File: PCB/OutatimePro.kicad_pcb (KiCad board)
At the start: 2 copper layers, 25.7 x 27.7 mm, 53 parts, among them IC1 PAM8904JPR, J1 USB_B_Micro_PCB_Edge_receptac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, J3 OSO_SWD, Q1 ALS-PT19-315C/L177/TR8, SW1 EVPAWED40, U1 ATSAML22N18A-CFUT, U2 MIC5365-3.3YMT, U3 USBLC6-2P6, U4 MAX40200ANS, U5 MAX40200ANS, U6 LIS2DW12TR, Y1 32.768kHz

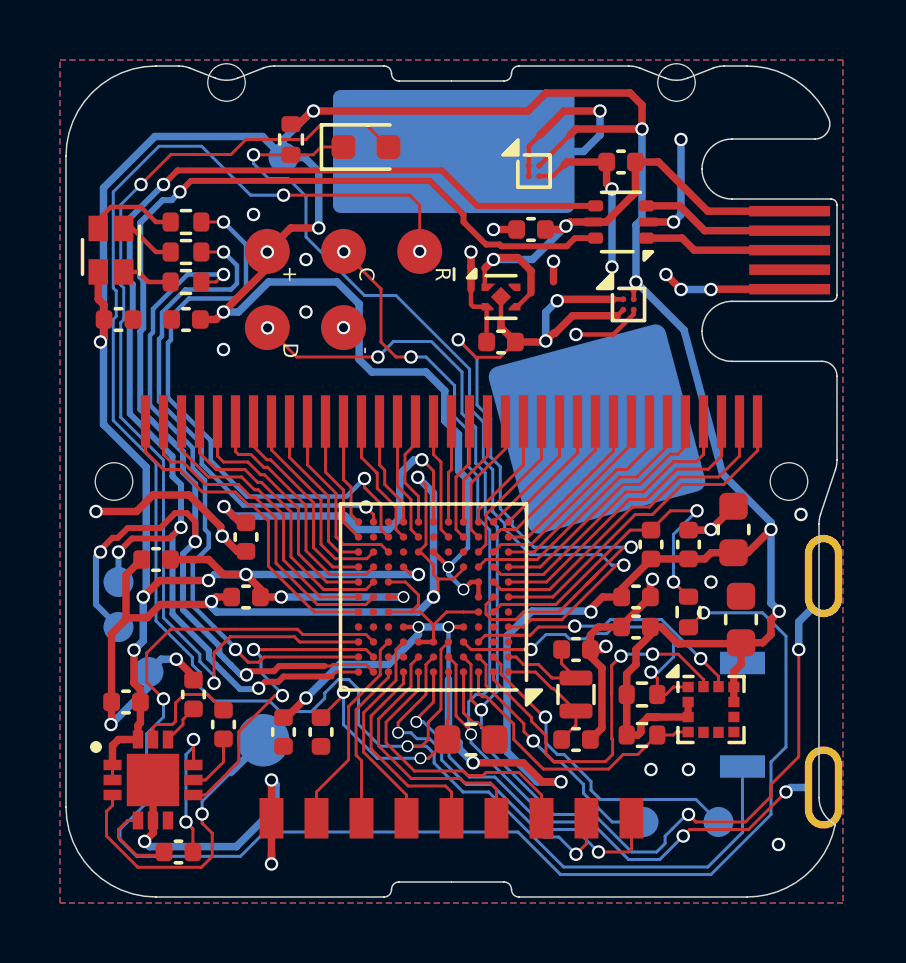
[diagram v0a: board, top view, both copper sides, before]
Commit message: move mcu to part where it fits & add promotional artwork
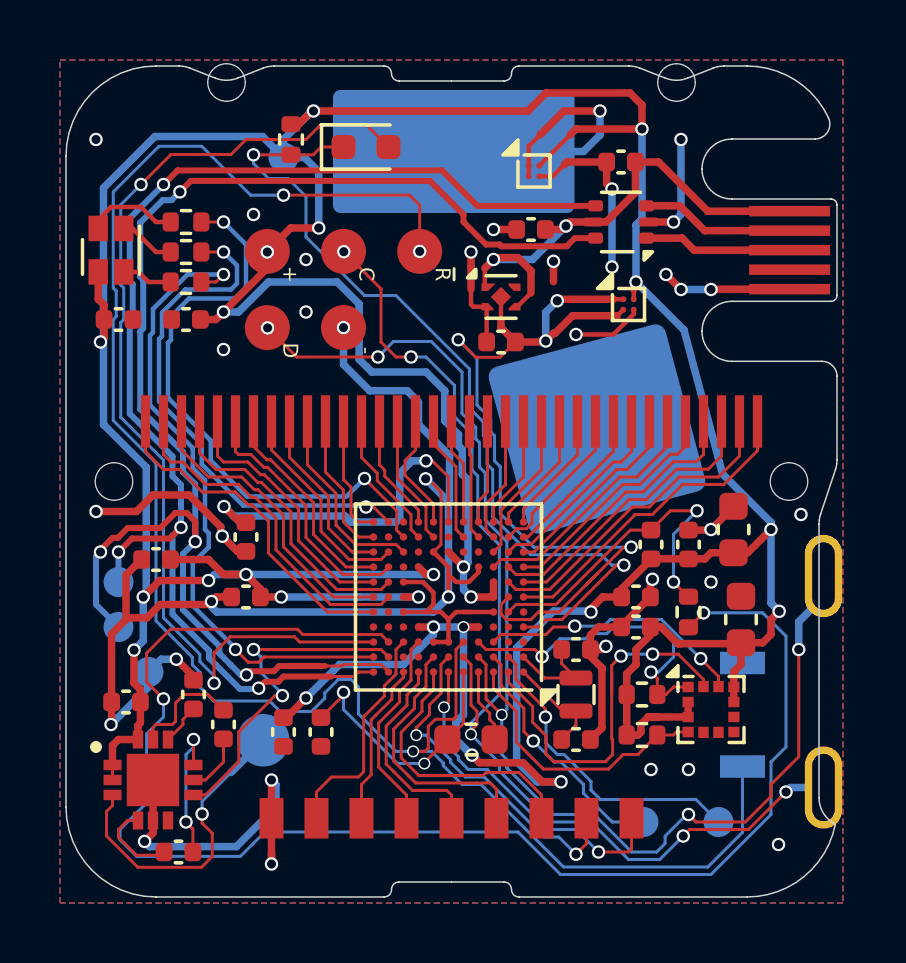
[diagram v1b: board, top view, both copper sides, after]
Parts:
- moved U1 0.50 mm to (25.8, 31.0)
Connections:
- LCD1 pad 34: /SEG39 -> /SEG29
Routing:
- net GND: track 86.5 -> 95.7 mm, vias 34 -> 35
- net VCC: track 164.8 -> 163.9 mm
- net /KPD_C3: track 12.1 -> 11.3 mm
- net /KPD_R3: track 6.87 -> 7.60 mm
- net /KPD_C2: track 12.1 -> 11.4 mm
- net /A3/D0/CS: track 9.57 -> 8.94 mm
- net /SEG25: track 8.80 -> 8.30 mm
- net /LIGHTSENSE: track 29.2 -> 28.7 mm
- net /USB_N: track 41.8 -> 42.3 mm
- net /SEG29: track 11.3 -> 10.8 mm
- net /XIN32: track 3.94 -> 3.44 mm
- net /SEG06: track 4.31 -> 4.81 mm
- net /XOUT32: track 3.69 -> 3.19 mm
- net /USB_P: track 46.2 -> 46.7 mm
- net /TEMPSENSE: track 11.6 -> 11.1 mm
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
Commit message: add critical components for reliable operation (datasheet sch. checklist)
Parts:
- added C22: 0.1uF, Capacitor_SMD:C_0402_1005Metric, F.Cu at (21.4, 35.5)
- added R12: 330, Resistor_SMD:R_0402_1005Metric, F.Cu at (35.0, 37.5)
- added R8: 10k, Resistor_SMD:R_0402_1005Metric, F.Cu at (19.4, 35.5)
- moved C8 0.90 mm to (22.4, 35.5)
- moved C11 0.15 mm to (20.4, 35.5)
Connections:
- SW1 pad 2: /~{RESET} -> Net-(R12-Pad1)
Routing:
- net /BTN_ADJUST: track 36.7 -> 57.7 mm
- net VCC: track 163.9 -> 166.3 mm
- net Net-(R12-Pad1): track 0.00 -> 2.05 mm, vias 0 -> 1
- net GND: track 95.7 -> 95.2 mm, vias 35 -> 34
- net /~{RESET}: track 60.7 -> 61.0 mm, vias 3 -> 5
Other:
- board text added: "v260920"
- board text removed: "v260907"

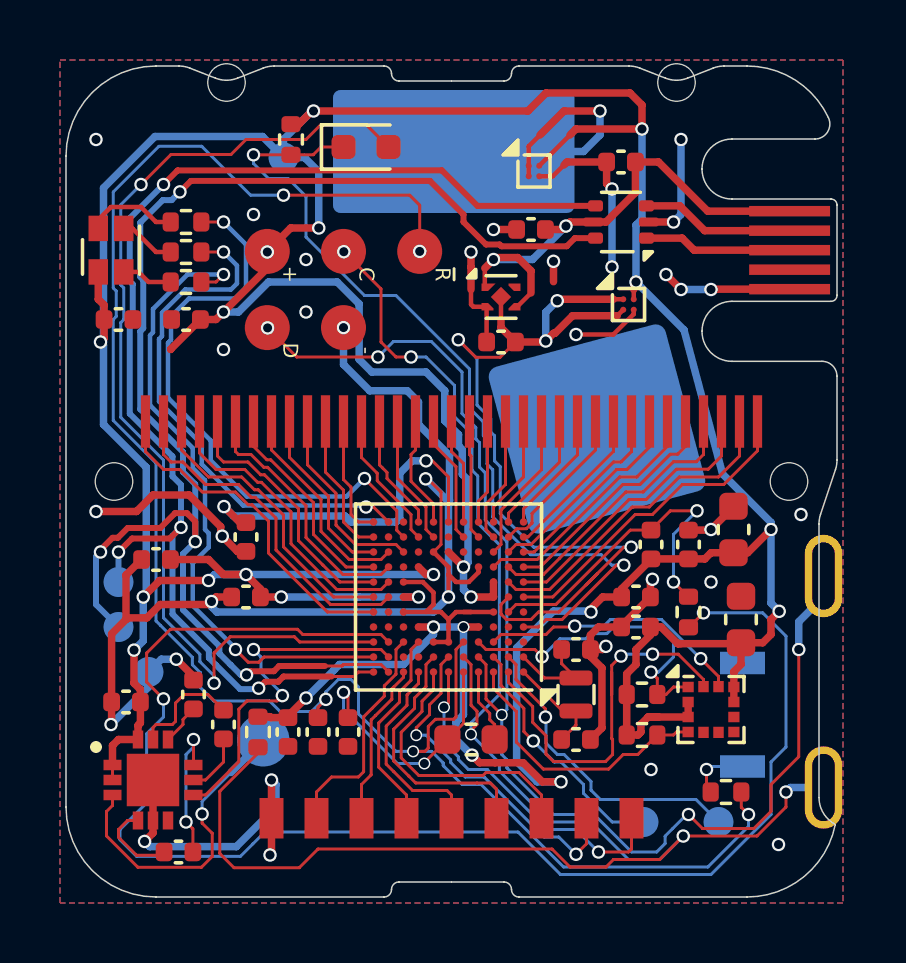
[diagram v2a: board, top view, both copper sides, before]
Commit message: Change programming header text size, change button pad copper size
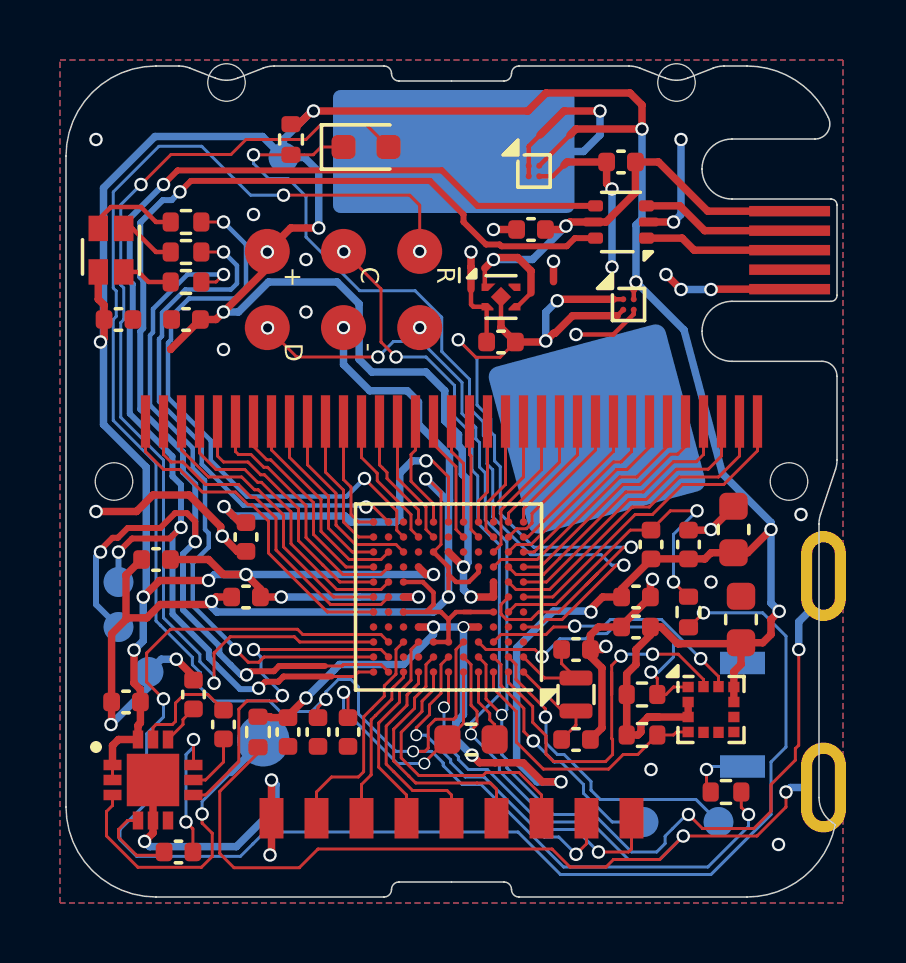
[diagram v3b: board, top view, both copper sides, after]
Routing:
- net (no net): vias 0 -> 1

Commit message: Update version number
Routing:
- net VCC: track 166.3 -> 166.9 mm
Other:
- board text added: "v261017"
- board text removed: "v260920"
